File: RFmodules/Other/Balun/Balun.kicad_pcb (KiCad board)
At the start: 2 copper layers, 4 parts, among them J1 SMA, J2 SMA, J3 SMA, U1 T

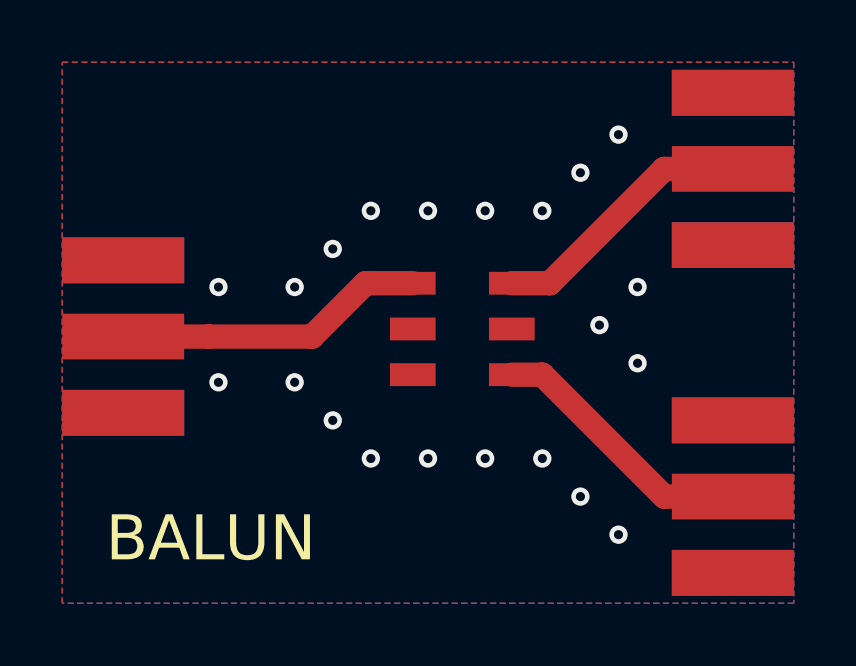
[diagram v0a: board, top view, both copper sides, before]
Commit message: Fix zone clearance, add description
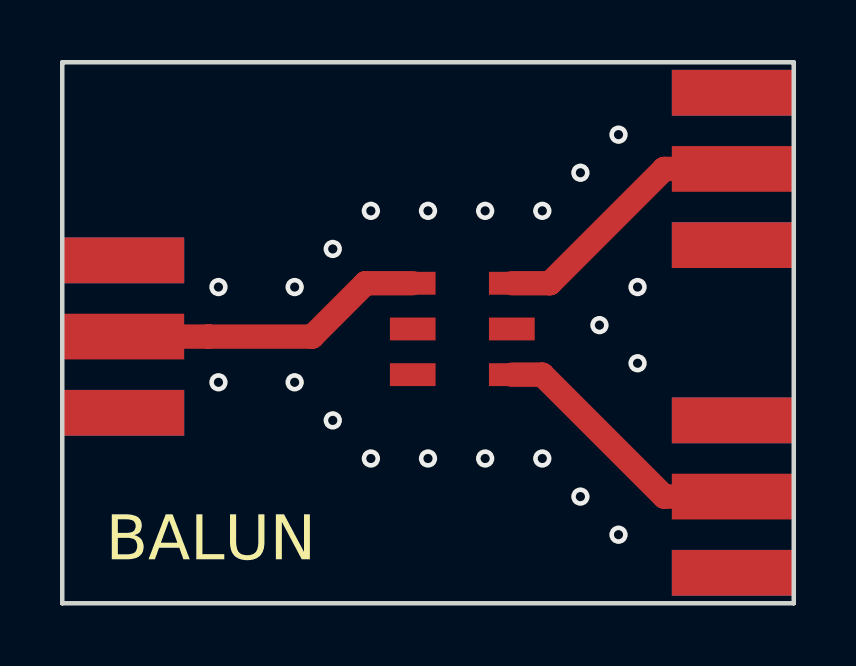
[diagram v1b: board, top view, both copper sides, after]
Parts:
- added REF**: OSHW-Logo2_7.3x6mm_SilkScreen, Symbol:OSHW-Logo2_7.3x6mm_SilkScreen, B.Cu at (81.1, 155.8)
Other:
- board outline added: 24.4 x 18 mm
- board text added: "Balun Revision 1 - 01/2019 github.com/fgaletsee/RFLego"
